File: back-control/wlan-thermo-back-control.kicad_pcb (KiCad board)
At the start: 2 copper layers, 36.2 x 43.2 mm, 13 parts, among them J1 AC / L, J2 AC / N, J3 Signal, J4 Front PWR, Q1 SS8050-G, U2 WX-DC12003, U3 PC817

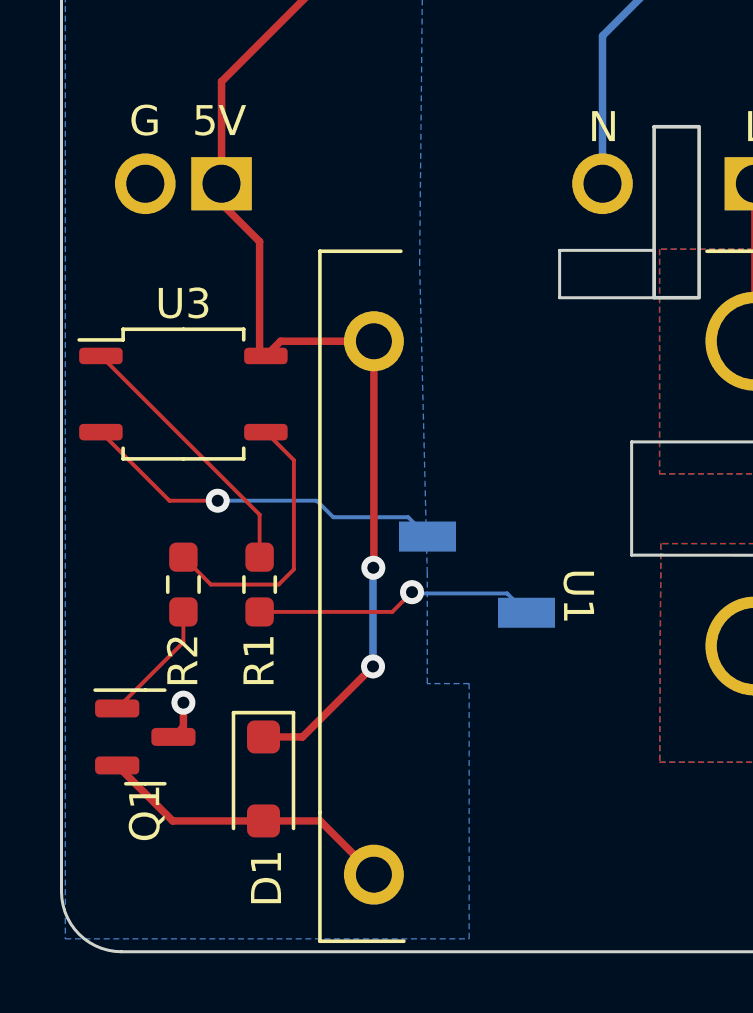
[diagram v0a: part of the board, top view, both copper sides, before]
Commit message: Revised optocopler footprint
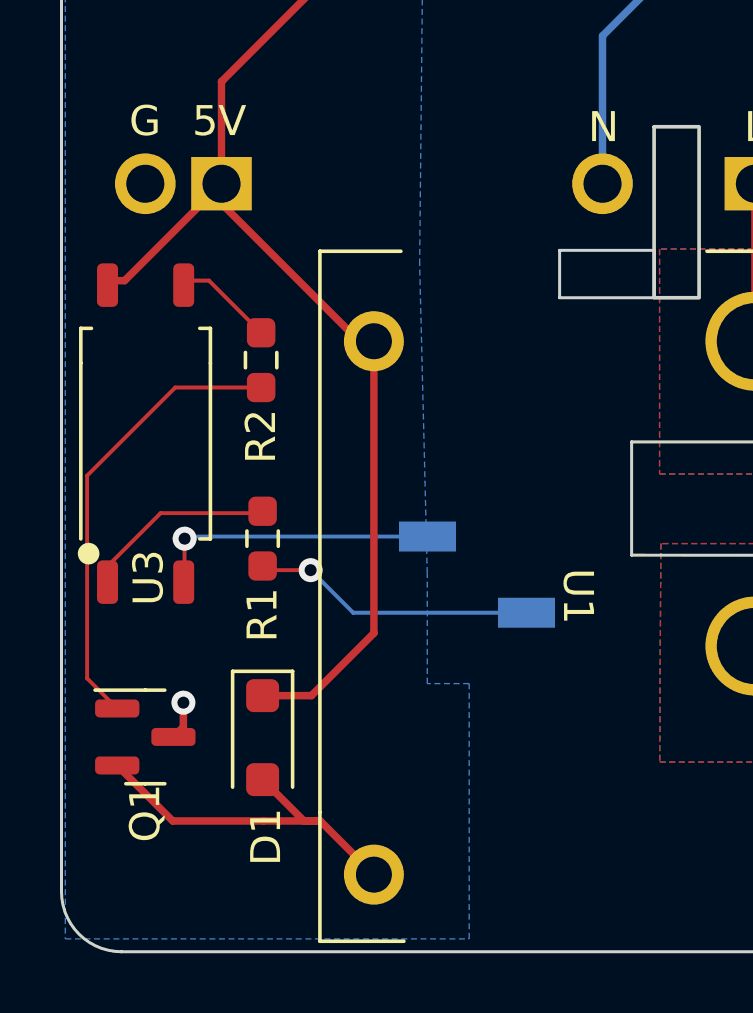
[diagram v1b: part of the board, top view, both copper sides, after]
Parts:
- U3: footprint Package_SO:SOP-4_3.8x4.1mm_P2.54mm -> Chof747 Footprints:SOP-4_6.7x4.1mm_P2.54mm
- moved R2 7.92 mm to (76.2, 92.8)
- moved U3 1.82 mm to (72.4, 95.3), turned to 90 degrees
- moved R1 1.53 mm to (76.3, 98.8)
- moved D1 1.38 mm to (76.3, 105.4)
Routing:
- net Net-(Q1-B): track 4.13 -> 15.2 mm
- net Net-(R2-Pad1): track 9.23 -> 3.30 mm
- net GND1: track 12.3 -> 9.69 mm
- net /RELAY_GND: track 10.1 -> 12.6 mm
- net Net-(R1-Pad2): track 8.90 -> 6.61 mm
- net +5V: track 43.7 -> 44.8 mm, vias 3 -> 1

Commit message: Redid whole for creeping protection of power supply
- Changed frontend connectors also to throughole pins
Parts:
- J3, J4: footprint Connector_PinSocket_2.54mm:PinSocket_1x02_P2.54mm_Vertical_SMD_Pin1Right -> Connector_PinSocket_2.54mm:PinSocket_1x02_P2.54mm_Vertical
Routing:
- net +5V: track 44.8 -> 42.1 mm, vias 1 -> 0
- net GND1: track 9.69 -> 11.9 mm
- net MC_SIGNAL: track 9.44 -> 8.32 mm
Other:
- outline, holes or cut-outs redrawn

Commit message: Merging of first revision round after component testing
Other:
- board text added: "W-Lan Thermo Back Control v1.1 (2023)"
- board text removed: "W-Lan Thermo Back Control v1.0 (2023)"
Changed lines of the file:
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@@
   (gr_arc (start 105.759 110.57) (mid 105.173214 111.984214) (end 103.759 112.57)
     (stroke (width 0.1) (type default)) (layer "Edge.Cuts"))
-  (gr_text "W-Lan Thermo Back Control\nv1.0 (2023)" (at 74.16 89.61 90) (layer "B.SilkS")
+  (gr_text "W-Lan Thermo Back Control\nv1.1 (2023)" (at 74.16 89.61 90) (layer "B.SilkS")
     (effects (font (size 1 1) (thickness 0.15)) (justify left bottom mirror))
   )

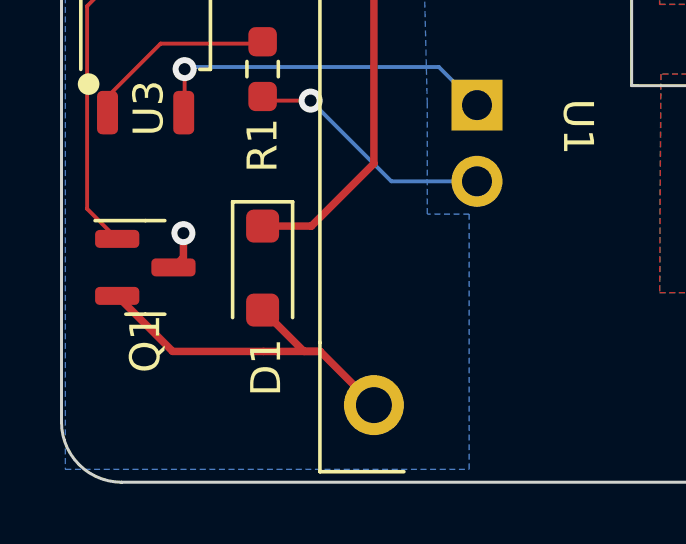
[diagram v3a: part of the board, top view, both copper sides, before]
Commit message: Correcrted relay switching transistor pins
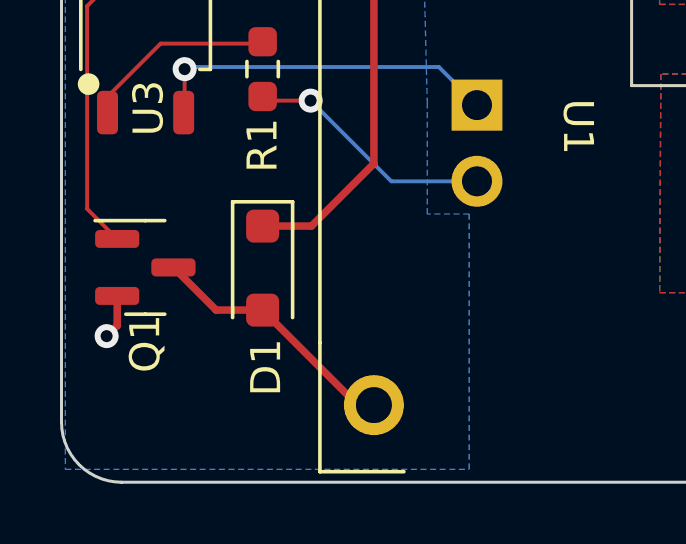
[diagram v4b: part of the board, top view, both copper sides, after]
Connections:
- Q1 pad 2: /RELAY_GND -> GND
- Q1 pad 3: GND -> /RELAY_GND
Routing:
- net /RELAY_GND: track 12.6 -> 8.58 mm
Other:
- board text added: "G1 SW"
- board text added: "GND 5V"
- board text added: "W-Lan Thermo Back Control v1.2 (2023)"
- board text removed: "W-Lan Thermo Back Control v1.1 (2023)"
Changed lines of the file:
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@@
     (property "Sheetfile" "wlan-thermo-back-control.kicad_sch")
     (property "Sheetname" "")
-    (property "ki_description" "NPN transistor, base/collector/emitter")
+    (property "ki_description" "NPN transistor, base/emitter/collector")
     (property "ki_keywords" "transistor NPN")
     (attr smd)
@@
       (net 8 "Net-(Q1-B)") (pinfunction "B") (pintype "input"))
     (pad "2" smd roundrect (at -0.9375 0.95) (size 1.475 0.6) (layers "F.Cu" "F.Paste" "F.Mask") (roundrect_rratio 0.25)
-      (net 2 "/RELAY_GND") (pinfunction "C") (pintype "passive"))
-    (pad "3" smd roundrect (at 0.9375 0) (size 1.475 0.6) (layers "F.Cu" "F.Paste" "F.Mask") (roundrect_rratio 0.25)
       (net 7 "GND") (pinfunction "E") (pintype "passive"))
+    (pad "3" smd roundrect (at 0.9375 0) (size 1.475 0.6) (layers "F.Cu" "F.Paste" "F.Mask") (roundrect_rratio 0.25)
+      (net 2 "/RELAY_GND") (pinfunction "C") (pintype "passive"))
     (model "${KICAD6_3DMODEL_DIR}/Package_TO_SOT_SMD.3dshapes/SOT-23.wrl"
       (offset (xyz 0 0 0))
@@
   (gr_arc (start 105.759 110.57) (mid 105.173214 111.984214) (end 103.759 112.57)
     (stroke (width 0.1) (type default)) (layer "Edge.Cuts"))
-  (gr_text "W-Lan Thermo Back Control\nv1.1 (2023)" (at 74.16 89.61 90) (layer "B.SilkS")
+  (gr_text "GND\n5V" (at 87.9 75.3) (layer "B.SilkS")
+    (effects (font (size 1 1) (thickness 0.15)) (justify left bottom mirror))
+  )
+  (gr_text "G1\nSW" (at 87.7 102.4) (layer "B.SilkS")
+    (effects (font (size 1 1) (thickness 0.15)) (justify left bottom mirror))
+  )
+  (gr_text "W-Lan Thermo Back Control\nv1.2 (2023)" (at 74.16 89.61 90) (layer "B.SilkS")
     (effects (font (size 1 1) (thickness 0.15)) (justify left bottom mirror))
   )
@@
   (segment (start 74.93 86.97) (end 74.93 83.566) (width 0.25) (layer "F.Cu") (net 1))
   (segment (start 76.3 104.0325) (end 77.9275 104.0325) (width 0.25) (layer "F.Cu") (net 1))
-  (segment (start 71.4525 106.36) (end 73.3025 108.21) (width 0.25) (layer "F.Cu") (net 2))
-  (segment (start 76.3 106.8325) (end 77.6775 108.21) (width 0.25) (layer "F.Cu") (net 2))
-  (segment (start 78.22 108.21) (end 80.01 110) (width 0.25) (layer "F.Cu") (net 2))
-  (segment (start 77.6775 108.21) (end 78.22 108.21) (width 0.25) (layer "F.Cu") (net 2))
-  (segment (start 76.33 108.21) (end 78.22 108.21) (width 0.25) (layer "F.Cu") (net 2))
-  (segment (start 73.3025 108.21) (end 76.33 108.21) (width 0.25) (layer "F.Cu") (net 2))
+  (segment (start 74.75 106.8325) (end 73.3275 105.41) (width 0.25) (layer "F.Cu") (net 2))
+  (segment (start 76.3 106.8325) (end 79.4675 110) (width 0.25) (layer "F.Cu") (net 2))
+  (segment (start 76.3 106.8325) (end 74.75 106.8325) (width 0.25) (layer "F.Cu") (net 2))
+  (segment (start 79.4675 110) (end 80.01 110) (width 0.25) (layer "F.Cu") (net 2))
   (via (at 97.02 100.696) (size 0.8) (drill 0.4) (layers "F.Cu" "B.Cu") (free) (net 3))
   (via (at 97.02 102.347) (size 0.8) (drill 0.4) (layers "F.Cu" "B.Cu") (free) (net 3))
@@
   (segment (start 77.9 99.85) (end 80.59 102.54) (width 0.13) (layer "B.Cu") (net 6))
   (segment (start 80.59 102.54) (end 83.445517 102.54) (width 0.13) (layer "B.Cu") (net 6))
-  (segment (start 73.66 105.0775) (end 73.3275 105.41) (width 0.25) (layer "F.Cu") (net 7))
-  (segment (start 73.66 104.267) (end 73.66 105.0775) (width 0.25) (layer "F.Cu") (net 7))
-  (via (at 73.66 104.267) (size 0.8) (drill 0.4) (layers "F.Cu" "B.Cu") (free) (net 7))
+  (segment (start 71.4525 107.3475) (end 71.1 107.7) (width 0.25) (layer "F.Cu") (net 7))
+  (segment (start 71.4525 106.36) (end 71.4525 107.3475) (width 0.25) (layer "F.Cu") (net 7))
+  (via (at 71.1 107.7) (size 0.8) (drill 0.4) (layers "F.Cu" "B.Cu") (free) (net 7))
   (segment (start 70.45 103.4575) (end 71.4525 104.46) (width 0.13) (layer "F.Cu") (net 8))
   (segment (start 70.45 96.7) (end 70.45 103.4575) (width 0.13) (layer "F.Cu") (net 8))
